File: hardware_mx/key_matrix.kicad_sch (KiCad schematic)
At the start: 170 parts, among them SW10 SW_SPST, SW11 SW_SPST, SW12 SW_SPST, SW13 SW_SPST, SW14 SW_SPST, SW15 SW_SPST, SW16 SW_SPST, SW17 SW_SPST, SW18 SW_SPST, SW19 SW_SPST, SW2 SW_SPST, SW20 SW_SPST, SW21 SW_SPST, SW22 SW_SPST, SW23 SW_SPST, SW24 SW_SPST, SW25 SW_SPST, SW26 SW_SPST, SW27 SW_SPST, SW28 SW_SPST, SW29 SW_SPST, SW3 SW_SPST, SW30 SW_SPST, SW31 SW_SPST, SW32 SW_SPST, SW33 SW_SPST, SW34 SW_SPST, SW35 SW_SPST, SW36 SW_SPST, SW37 SW_SPST, SW38 SW_SPST, SW39 SW_SPST, SW4 SW_SPST, SW40 SW_SPST, SW41 SW_SPST, SW42 SW_SPST, SW43 SW_SPST, SW44 SW_SPST, SW45 SW_SPST, SW46 SW_SPST, SW47 SW_SPST, SW48 SW_SPST, SW49 SW_SPST, SW5 SW_SPST, SW50 SW_SPST, SW51 SW_SPST, SW52 SW_SPST, SW53 SW_SPST, SW54 SW_SPST, SW55 SW_SPST, SW56 SW_SPST, SW57 SW_SPST, SW58 SW_SPST, SW59 SW_SPST, SW6 SW_SPST, SW60 SW_SPST, SW61 SW_SPST, SW62 SW_SPST, SW63 SW_SPST, SW64 SW_SPST, SW65 SW_SPST, SW66 SW_SPST, SW67 SW_SPST, SW68 SW_SPST, SW69 SW_SPST, SW7 SW_SPST, SW70 SW_SPST, SW71 SW_SPST, SW72 SW_SPST, SW73 SW_SPST, SW75 SW_SPST, SW76 SW_SPST, SW77 SW_SPST, SW78 SW_SPST, SW79 SW_SPST, SW8 SW_SPST, SW80 SW_SPST, SW81 SW_SPST, SW82 SW_SPST, SW9 SW_SPST

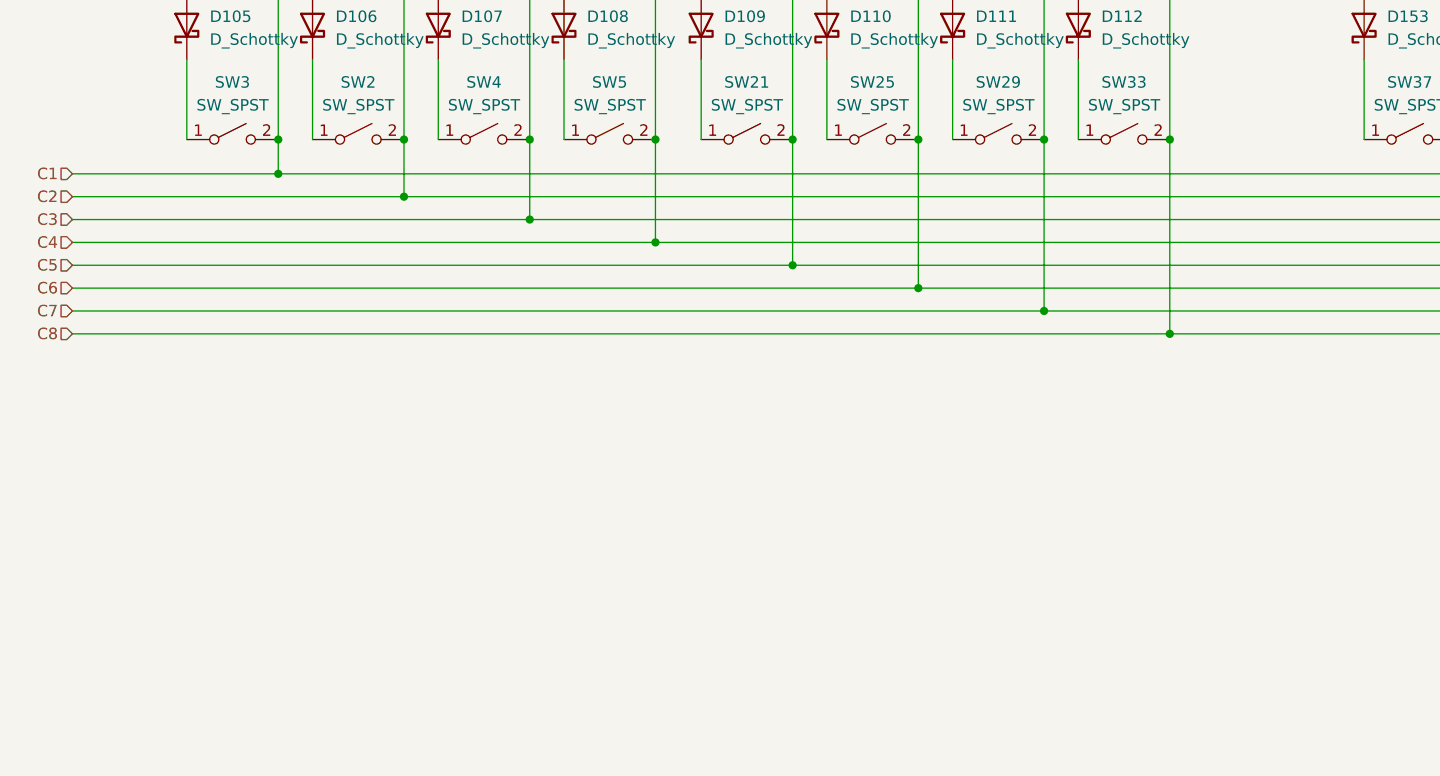
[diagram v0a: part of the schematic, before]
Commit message: Add mosfets to columns
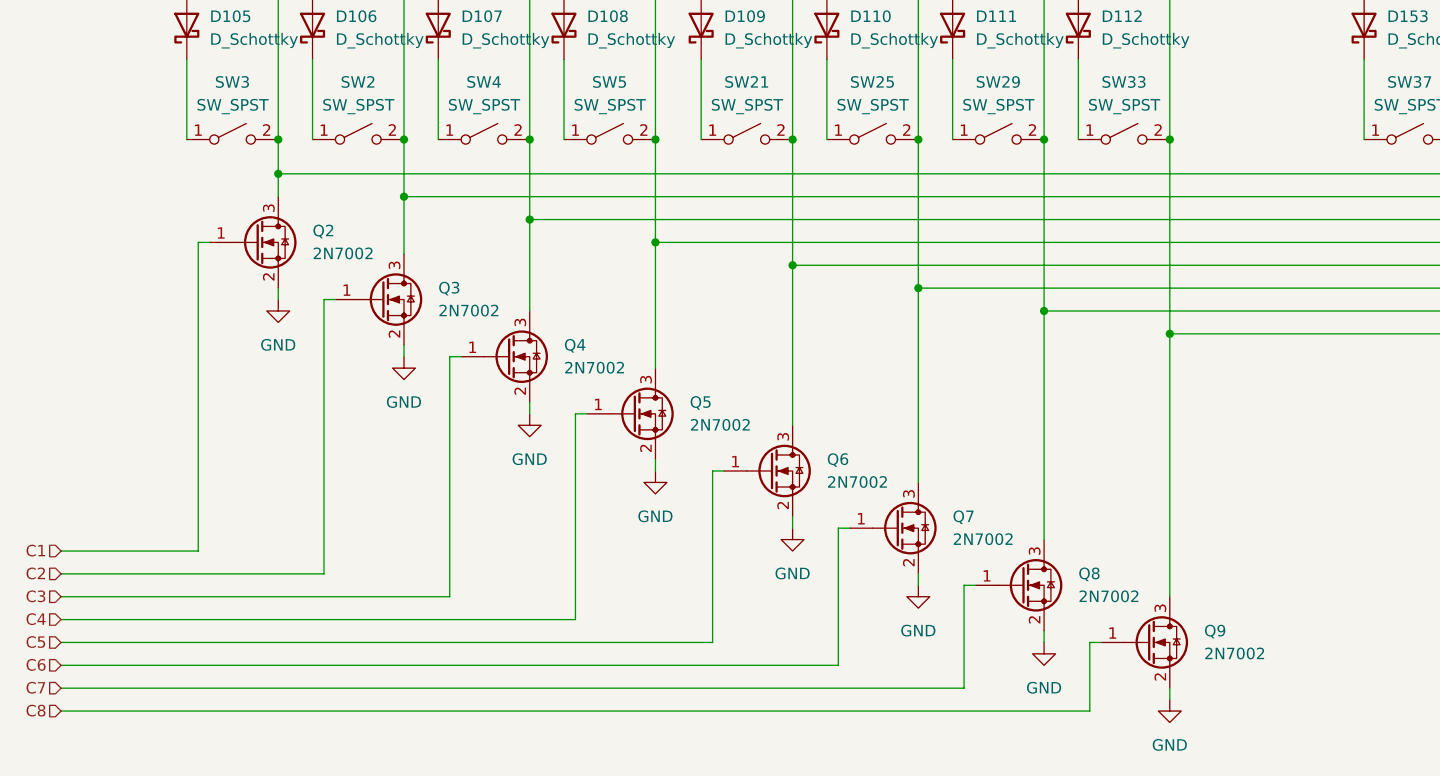
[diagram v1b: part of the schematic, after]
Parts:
- added Q2, Q3, Q4, Q5, Q6, Q7, Q8, Q9: 2N7002, Package_TO_SOT_SMD:SOT-23, symbol Transistor_FET:2N7002
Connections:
- net C1: now also Q2.1 (G); no longer SW10.2 (B), SW11.2 (B), SW3.2 (B), SW34.2 (B), SW35.2 (B), SW36.2 (B), SW37.2 (B), SW6.2 (B), SW66.2 (B), SW75.2 (B)
- net C2: now also Q3.1 (G); no longer SW12.2 (B), SW13.2 (B), SW2.2 (B), SW38.2 (B), SW39.2 (B), SW40.2 (B), SW41.2 (B), SW67.2 (B), SW7.2 (B), SW76.2 (B)
- net C3: now also Q4.1 (G); no longer SW14.2 (B), SW15.2 (B), SW4.2 (B), SW42.2 (B), SW43.2 (B), SW44.2 (B), SW45.2 (B), SW68.2 (B), SW77.2 (B), SW8.2 (B)
- net C4: now also Q5.1 (G); no longer SW16.2 (B), SW17.2 (B), SW46.2 (B), SW47.2 (B), SW48.2 (B), SW49.2 (B), SW5.2 (B), SW69.2 (B), SW78.2 (B), SW9.2 (B)
- net C5: now also Q6.1 (G); no longer SW18.2 (B), SW19.2 (B), SW20.2 (B), SW21.2 (B), SW50.2 (B), SW51.2 (B), SW52.2 (B), SW53.2 (B), SW70.2 (B), SW79.2 (B)
- net C6: now also Q7.1 (G); no longer SW22.2 (B), SW23.2 (B), SW24.2 (B), SW25.2 (B), SW54.2 (B), SW55.2 (B), SW56.2 (B), SW57.2 (B), SW71.2 (B), SW80.2 (B)
- net C7: now also Q8.1 (G); no longer SW26.2 (B), SW27.2 (B), SW28.2 (B), SW29.2 (B), SW58.2 (B), SW59.2 (B), SW60.2 (B), SW61.2 (B), SW72.2 (B), SW81.2 (B)
- net C8: now also Q9.1 (G); no longer SW30.2 (B), SW31.2 (B), SW32.2 (B), SW33.2 (B), SW62.2 (B), SW63.2 (B), SW64.2 (B), SW65.2 (B), SW73.2 (B), SW82.2 (B)
- new net: Q7.3 (D), SW22.2 (B), SW23.2 (B), SW24.2 (B), SW25.2 (B), SW54.2 (B), SW55.2 (B), SW56.2 (B), SW57.2 (B), SW71.2 (B), SW80.2 (B)
- new net: Q9.3 (D), SW30.2 (B), SW31.2 (B), SW32.2 (B), SW33.2 (B), SW62.2 (B), SW63.2 (B), SW64.2 (B), SW65.2 (B), SW73.2 (B), SW82.2 (B)
- new net: Q6.3 (D), SW18.2 (B), SW19.2 (B), SW20.2 (B), SW21.2 (B), SW50.2 (B), SW51.2 (B), SW52.2 (B), SW53.2 (B), SW70.2 (B), SW79.2 (B)
- new net: Q8.3 (D), SW26.2 (B), SW27.2 (B), SW28.2 (B), SW29.2 (B), SW58.2 (B), SW59.2 (B), SW60.2 (B), SW61.2 (B), SW72.2 (B), SW81.2 (B)
- new net: Q2.3 (D), SW10.2 (B), SW11.2 (B), SW3.2 (B), SW34.2 (B), SW35.2 (B), SW36.2 (B), SW37.2 (B), SW6.2 (B), SW66.2 (B), SW75.2 (B)
- new net: Q5.3 (D), SW16.2 (B), SW17.2 (B), SW46.2 (B), SW47.2 (B), SW48.2 (B), SW49.2 (B), SW5.2 (B), SW69.2 (B), SW78.2 (B), SW9.2 (B)
- new net: Q3.3 (D), SW12.2 (B), SW13.2 (B), SW2.2 (B), SW38.2 (B), SW39.2 (B), SW40.2 (B), SW41.2 (B), SW67.2 (B), SW7.2 (B), SW76.2 (B)
- new net: Q4.3 (D), SW14.2 (B), SW15.2 (B), SW4.2 (B), SW42.2 (B), SW43.2 (B), SW44.2 (B), SW45.2 (B), SW68.2 (B), SW77.2 (B), SW8.2 (B)
- new net GND: Q2.2 (S), Q3.2 (S), Q4.2 (S), Q5.2 (S), Q6.2 (S), Q7.2 (S), Q8.2 (S), Q9.2 (S)
